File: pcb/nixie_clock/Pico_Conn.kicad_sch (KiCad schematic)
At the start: 1 part, among them U14 PicoW

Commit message: remove busses and output stuff
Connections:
- net Nixie_EN renamed Nixie_Clk
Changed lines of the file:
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@@
 		)
 	)
-	(hierarchical_label "Nixie_EN"
+	(hierarchical_label "Nixie_Clk"
 		(shape output)
 		(at 123.19 60.96 180)

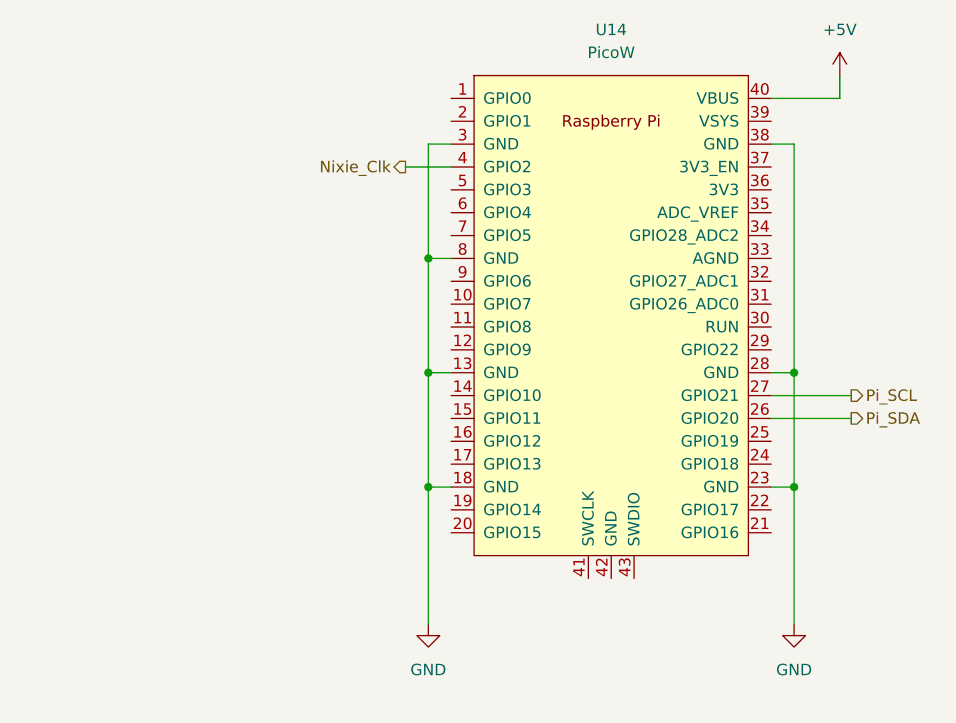
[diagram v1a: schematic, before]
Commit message: schematic finalisation, footprint assignment and start on placeing components in layout.
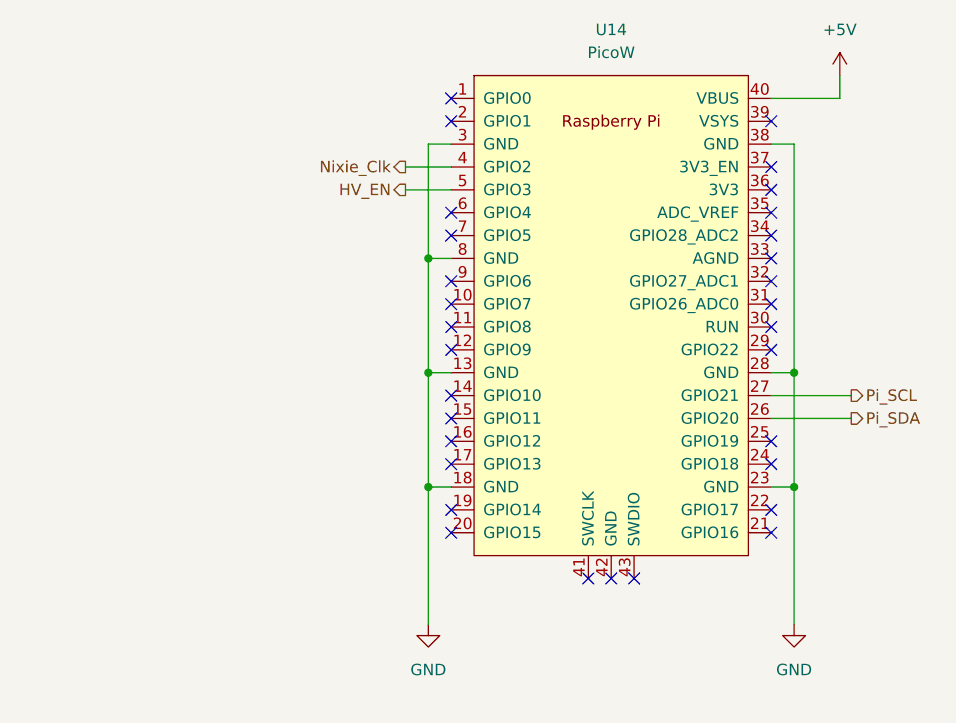
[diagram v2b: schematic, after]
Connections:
- net HV_EN: now reaches U14.5 (GPIO3)
- no-connect marks 0 -> 31
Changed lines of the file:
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@@
 		(color 0 0 0 0)
 	)
+	(no_connect
+		(at 163.83 81.28)
+	)
+	(no_connect
+		(at 163.83 78.74)
+	)
+	(no_connect
+		(at 128.27 53.34)
+	)
+	(no_connect
+		(at 163.83 93.98)
+	)
+	(no_connect
+		(at 128.27 86.36)
+	)
+	(no_connect
+		(at 128.27 55.88)
+	)
+	(no_connect
+		(at 128.27 66.04)
+	)
+	(no_connect
+		(at 163.83 91.44)
+	)
+	(no_connect
+		(at 128.27 93.98)
+	)
+	(no_connect
+		(at 163.83 73.66)
+	)
+	(no_connect
+		(at 163.83 55.88)
+	)
+	(no_connect
+		(at 128.27 91.44)
+	)
+	(no_connect
+		(at 128.27 101.6)
+	)
+	(no_connect
+		(at 163.83 68.58)
+	)
+	(no_connect
+		(at 146.05 106.68)
+	)
+	(no_connect
+		(at 128.27 76.2)
+	)
+	(no_connect
+		(at 128.27 81.28)
+	)
+	(no_connect
+		(at 163.83 76.2)
+	)
+	(no_connect
+		(at 163.83 99.06)
+	)
+	(no_connect
+		(at 163.83 101.6)
+	)
+	(no_connect
+		(at 148.59 106.68)
+	)
+	(no_connect
+		(at 163.83 71.12)
+	)
+	(no_connect
+		(at 128.27 99.06)
+	)
+	(no_connect
+		(at 128.27 88.9)
+	)
+	(no_connect
+		(at 128.27 73.66)
+	)
+	(no_connect
+		(at 128.27 68.58)
+	)
+	(no_connect
+		(at 143.51 106.68)
+	)
+	(no_connect
+		(at 163.83 63.5)
+	)
+	(no_connect
+		(at 163.83 60.96)
+	)
+	(no_connect
+		(at 128.27 78.74)
+	)
+	(no_connect
+		(at 163.83 66.04)
+	)
 	(wire
 		(pts
@@
 	(wire
 		(pts
+			(xy 123.19 63.5) (xy 128.27 63.5)
+		)
+		(stroke
+			(width 0)
+			(type default)
+		)
+	)
+	(wire
+		(pts
 			(xy 171.45 50.8) (xy 171.45 53.34)
 		)
@@
 		)
 	)
+	(hierarchical_label "HV_EN"
+		(shape output)
+		(at 123.19 63.5 180)
+		(fields_autoplaced yes)
+		(effects
+			(font
+				(size 1.27 1.27)
+			)
+			(justify right)
+		)
+	)

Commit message: finalization of schematic (might add fuze on 170v supply) looking at pcb routing now. Decided on 6 layers.
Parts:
- U14: footprint RPi_PicoW:RPi_Pico_SMD_TH -> RPi_Pico:RPi_PicoW_SMD
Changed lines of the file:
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@@
 			)
 		)
-		(property "Footprint" "RPi_PicoW:RPi_Pico_SMD_TH"
+		(property "Footprint" "RPi_Pico:RPi_PicoW_SMD"
 			(at 146.05 77.47 90)
 			(effects
@@
 		(pin "37"
 		)
-		(pin "42"
-		)
 		(pin "40"
 		)
@@
 		(pin "36"
 		)
-		(pin "41"
-		)
 		(pin "9"
 		)
-		(pin "43"
-		)
 		(pin "13"

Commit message: 3d models done
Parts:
- U14: LCSC Part # (none) -> C7203003
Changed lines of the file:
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@@
+			)
+		)
+		(property "LCSC Part #" "C7203003"
+			(at 146.05 77.47 0)
+			(effects
+				(font
+					(size 1.27 1.27)
+				)
+				(hide yes)
 			)
 		)

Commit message: fixing some issues.
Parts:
- U14: now not fitted
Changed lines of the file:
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@@
 		(in_bom yes)
 		(on_board yes)
-		(dnp no)
+		(dnp yes)
 		(fields_autoplaced yes)
 		(property "Reference" "U14"

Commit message: added grounding
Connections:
- no-connect marks 31 -> 28
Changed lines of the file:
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@@
-	)
-	(no_connect
-		(at 128.27 66.04)
 	)
 	(no_connect
@@
 	)
 	(no_connect
+		(at 128.27 76.2)
+	)
+	(no_connect
 		(at 128.27 91.44)
 	)
@@
 	(no_connect
 		(at 163.83 68.58)
-	)
-	(no_connect
-		(at 146.05 106.68)
-	)
-	(no_connect
-		(at 128.27 76.2)
-	)
-	(no_connect
-		(at 128.27 81.28)
 	)
 	(no_connect
@@
 	)
 	(no_connect
-		(at 148.59 106.68)
+		(at 128.27 68.58)
+	)
+	(no_connect
+		(at 128.27 78.74)
 	)
 	(no_connect
@@
 	)
 	(no_connect
-		(at 128.27 73.66)
-	)
-	(no_connect
-		(at 128.27 68.58)
-	)
-	(no_connect
-		(at 143.51 106.68)
+		(at 128.27 66.04)
 	)
 	(no_connect
@@
 	)
 	(no_connect
-		(at 163.83 60.96)
+		(at 128.27 81.28)
 	)
 	(no_connect
-		(at 128.27 78.74)
+		(at 163.83 60.96)
 	)
 	(no_connect
 		(at 163.83 66.04)
 	)
+	(no_connect
+		(at 128.27 73.66)
+	)
 	(wire

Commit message: final commits before sending to jlc
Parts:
- added S1, S2, S3: SKRTLAE010, SKRTLAE010:SW_SKRTLAE010, symbol SKRTLAE010:SKRTLAE010
- U14: now fitted; now left out of the parts list
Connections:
- net GND: now also S1.1, S1.3, S2.1, S2.3, S3.1, S3.3
- net at U14.10 (GPIO7): now also S2.2
- net at U14.11 (GPIO8): now also S3.2
- net +3V3: now reaches U14.36 (3V3)
- net at U14.9 (GPIO6): now also S1.2
- no-connect marks 28 -> 30
